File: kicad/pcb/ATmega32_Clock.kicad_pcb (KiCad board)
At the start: 2 copper layers, 80 x 60 mm, 20 parts, among them J1 USART, J2 ISP, SW1 RESET, SW2 SET, SW3 INCREMENT, SW4 CLOCK_RESET, U1 ATmega32-16PU, Y1 8MHz

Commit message: Fix PCB: remove bad tracks (0 shorts), fix board outline (100x60mm), space buttons apart, regenerate Gerbers
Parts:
- moved R4 18.0 mm to (88.0, 42.0)
- moved SW4 18.0 mm to (90.0, 50.0)
- moved R3 10.0 mm to (73.0, 42.0)
- moved SW3 10.0 mm to (75.0, 50.0)
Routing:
- net SET_BTN: track 50.6 -> 0.00 mm
- net CLOCK_RESET: track 49.9 -> 0.00 mm
- net INC_BTN: track 49.7 -> 0.00 mm
- net MOSI: track 46.0 -> 0.00 mm
- net SCK: track 44.6 -> 0.00 mm
- net MISO: track 44.6 -> 0.00 mm
- net USART_TXD: track 39.7 -> 0.00 mm
- net USART_RXD: track 39.1 -> 0.00 mm
- net LED_TASK: track 31.9 -> 0.00 mm
- net GND: track 29.5 -> 0.00 mm
- net LED_STATUS: track 25.1 -> 0.00 mm
- net VCC: track 23.2 -> 0.00 mm
- net XTAL1: track 20.5 -> 0.00 mm
- net ~{RESET}: track 20.2 -> 0.00 mm
- net XTAL2: track 15.1 -> 0.00 mm
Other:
- board size 80 x 60 mm -> 100 x 60 mm
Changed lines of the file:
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@@
   (gr_rect
     (start 0 0)
-    (end 80 60)
+    (end 100 60)
     (stroke (width 0.15) (type solid))
     (fill none)
@@
     (stroke (width 0.15) (type solid))
     (fill none)
-    (layer "Edge.Cuts")
+    (layer "F.Fab")
   )
   (gr_circle
-    (center 76.5 3.5)
-    (end 78.1 3.5)
+    (center 96.5 3.5)
+    (end 98.1 3.5)
     (stroke (width 0.15) (type solid))
     (fill none)
-    (layer "Edge.Cuts")
+    (layer "F.Fab")
   )
   (gr_circle
@@
     (stroke (width 0.15) (type solid))
     (fill none)
-    (layer "Edge.Cuts")
+    (layer "F.Fab")
   )
   (gr_circle
-    (center 76.5 56.5)
-    (end 78.1 56.5)
+    (center 96.5 56.5)
+    (end 98.1 56.5)
     (stroke (width 0.15) (type solid))
     (fill none)
-    (layer "Edge.Cuts")
+    (layer "F.Fab")
   )
   (gr_text "ATmega32 Digital Clock"
@@
   (footprint "Resistor_THT:R_Axial_DIN0207_L6.3mm_D2.5mm_P10.16mm_Horizontal"
     (layer "F.Cu")
-    (at 63 42)
+    (at 73 42)
     (fp_text reference "R3"
       (at 5.08 -2 0)
@@
   (footprint "Button_Switch_THT:SW_PUSH_6mm"
     (layer "F.Cu")
-    (at 65 50)
+    (at 75 50)
     (fp_text reference "SW3"
       (at 3 -4 0)
@@
   (footprint "Resistor_THT:R_Axial_DIN0207_L6.3mm_D2.5mm_P10.16mm_Horizontal"
     (layer "F.Cu")
-    (at 70 42)
+    (at 88 42)
     (fp_text reference "R4"
       (at 5.08 -2 0)
@@
   (footprint "Button_Switch_THT:SW_PUSH_6mm"
     (layer "F.Cu")
-    (at 72 50)
+    (at 90 50)
     (fp_text reference "SW4"
       (at 3 -4 0)
@@
     (pad "6" thru_hole oval (at 2.54 5.08 0) (size 1.7 1.7) (drill 1.0) (layers "*.Cu" "*.Mask") (net 15 "SCK"))
   )
-  (segment (start 35 22.86) (end 27 14) (width 0.5) (layer "F.Cu") (net 1) (tstamp "t1000001-0000-4000-8000-000000000001"))
-  (segment (start 35 22.86) (end 42 14) (width 0.5) (layer "F.Cu") (net 1) (tstamp "t1000002-0000-4000-8000-000000000001"))
-  (segment (start 35 25.4) (end 16.5 28) (width 0.5) (layer "F.Cu") (net 2) (tstamp "t1000003-0000-4000-8000-000000000001"))
-  (segment (start 35 25.4) (end 24.5 28) (width 0.5) (layer "F.Cu") (net 2) (tstamp "t1000004-0000-4000-8000-000000000001"))
-  (segment (start 15.56 24) (end 35 30.48) (width 0.25) (layer "F.Cu") (net 10) (tstamp "t1000005-0000-4000-8000-000000000001"))
-  (segment (start 20.44 24) (end 35 27.94) (width 0.25) (layer "F.Cu") (net 11) (tstamp "t1000006-0000-4000-8000-000000000001"))
-  (segment (start 20.16 34) (end 35 20.32) (width 0.25) (layer "F.Cu") (net 12) (tstamp "t1000007-0000-4000-8000-000000000001"))
-  (segment (start 35 0) (end 58 10) (width 0.25) (layer "F.Cu") (net 6) (tstamp "t1000008-0000-4000-8000-000000000001"))
-  (segment (start 35 2.54) (end 66 10) (width 0.25) (layer "F.Cu") (net 7) (tstamp "t1000009-0000-4000-8000-000000000001"))
-  (segment (start 50.24 0) (end 58 50) (width 0.25) (layer "B.Cu") (net 3) (tstamp "t100000a-0000-4000-8000-000000000001"))
-  (segment (start 50.24 2.54) (end 65 50) (width 0.25) (layer "B.Cu") (net 4) (tstamp "t100000b-0000-4000-8000-000000000001"))
-  (segment (start 50.24 5.08) (end 72 50) (width 0.25) (layer "B.Cu") (net 5) (tstamp "t100000c-0000-4000-8000-000000000001"))
-  (segment (start 35 35.56) (end 74 28) (width 0.25) (layer "F.Cu") (net 8) (tstamp "t100000d-0000-4000-8000-000000000001"))
-  (segment (start 35 33.02) (end 74 30.54) (width 0.25) (layer "F.Cu") (net 9) (tstamp "t100000e-0000-4000-8000-000000000001"))
-  (segment (start 35 12.7) (end 8 50) (width 0.25) (layer "B.Cu") (net 13) (tstamp "t100000f-0000-4000-8000-000000000001"))
-  (segment (start 35 15.24) (end 10.54 52.54) (width 0.25) (layer "B.Cu") (net 14) (tstamp "t1000010-0000-4000-8000-000000000001"))
-  (segment (start 35 17.78) (end 10.54 55.08) (width 0.25) (layer "B.Cu") (net 15) (tstamp "t1000011-0000-4000-8000-000000000001"))
   (zone
     (net 2)
@@
     (polygon
       (pts
-        (xy 1 1)
-        (xy 79 1)
-        (xy 79 59)
-        (xy 1 59)
+        (xy -2 -2)
+        (xy 96 -2)
+        (xy 96 57)
+        (xy -2 57)
       )
     )

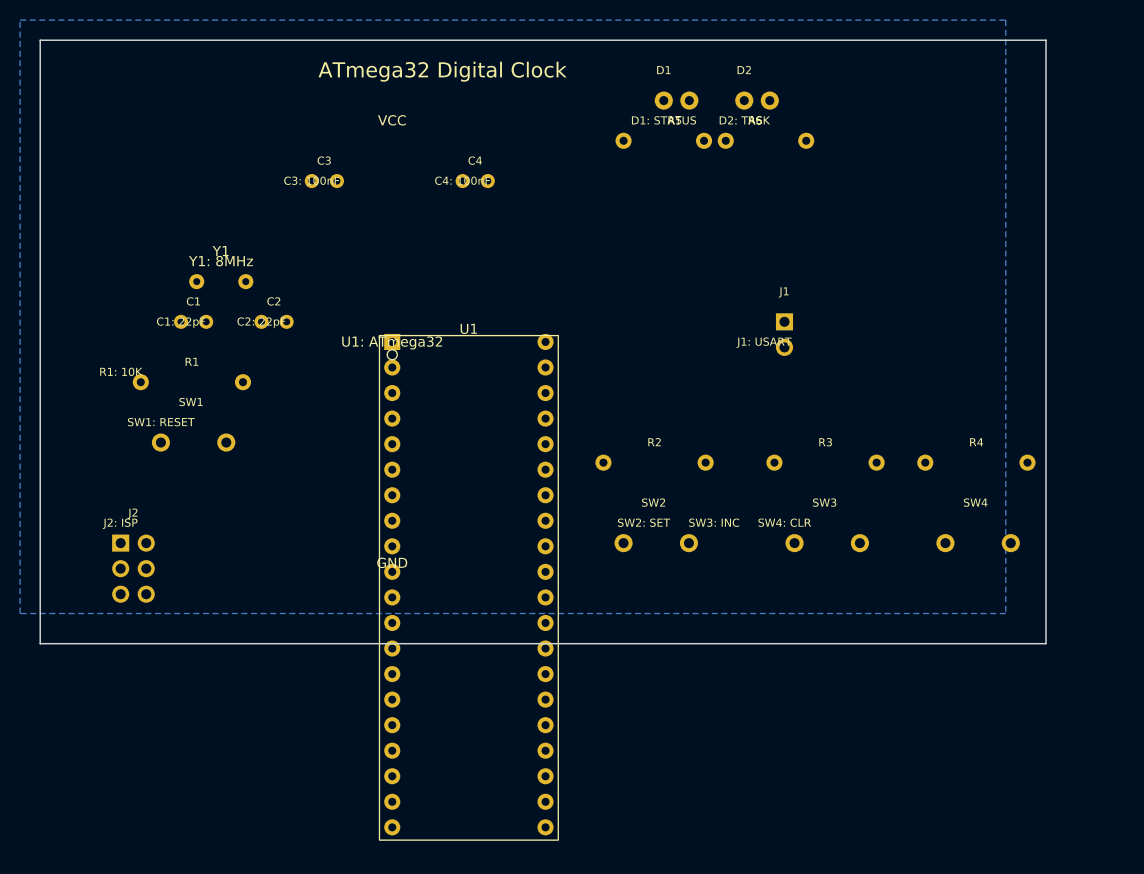
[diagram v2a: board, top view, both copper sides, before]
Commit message: Replace schematic and PCB with user's correct KiCad designs (0 ERC errors), update documentation
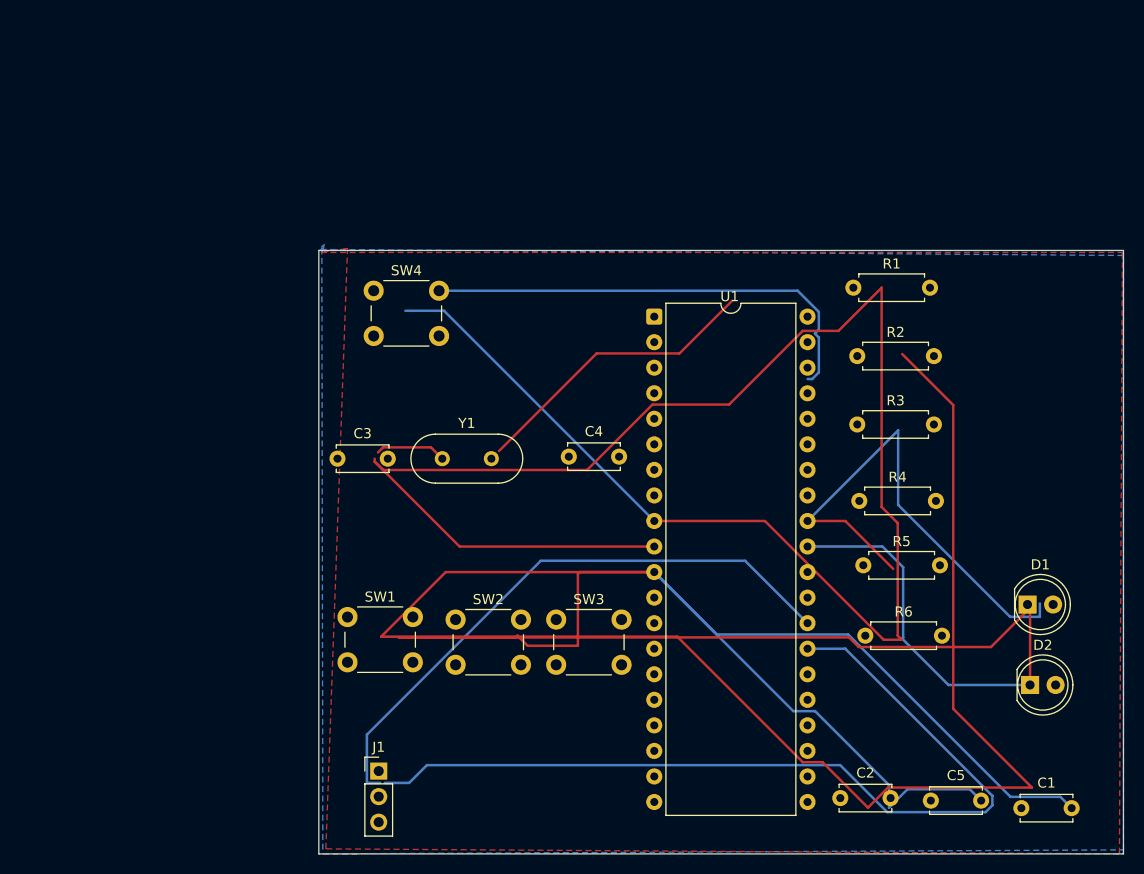
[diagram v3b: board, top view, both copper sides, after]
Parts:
- removed J2: ISP, Connector_PinHeader_2.54mm:PinHeader_2x03_P2.54mm_Vertical
- added C5: 100nF, Capacitor_THT:C_Disc_D5.0mm_W2.5mm_P5.00mm, F.Cu at (88.5, 75.6)
- C1, C2: value 22pF -> 100nF; footprint Capacitor_THT:C_Disc_D3.0mm_W1.6mm_P2.50mm -> Capacitor_THT:C_Disc_D5.0mm_W2.5mm_P5.00mm
- C3, C4: value 100nF -> 22pF; footprint Capacitor_THT:C_Disc_D3.0mm_W1.6mm_P2.50mm -> Capacitor_THT:C_Disc_D5.0mm_W2.5mm_P5.00mm
- D1: value LED_STATUS -> LED; footprint LED_THT:LED_D3.0mm -> LED_THT:LED_D5.0mm
- D2: value LED_TASK -> LED; footprint LED_THT:LED_D3.0mm -> LED_THT:LED_D5.0mm
- J1: value USART -> Conn_01x03_Pin; footprint Connector_PinHeader_2.54mm:PinHeader_1x02_P2.54mm_Vertical -> Connector_PinHeader_2.54mm:PinHeader_1x03_P2.54mm_Vertical
- R1, R2, R4: value 10K -> 10k; footprint Resistor_THT:R_Axial_DIN0207_L6.3mm_D2.5mm_P10.16mm_Horizontal -> Resistor_THT:R_Axial_DIN0207_L6.3mm_D2.5mm_P7.62mm_Horizontal
- R3: value 10K -> 220; footprint Resistor_THT:R_Axial_DIN0207_L6.3mm_D2.5mm_P10.16mm_Horizontal -> Resistor_THT:R_Axial_DIN0207_L6.3mm_D2.5mm_P7.62mm_Horizontal
- R5: value 330R -> 220; footprint Resistor_THT:R_Axial_DIN0207_L6.3mm_D2.5mm_P10.16mm_Horizontal -> Resistor_THT:R_Axial_DIN0207_L6.3mm_D2.5mm_P7.62mm_Horizontal
- R6: value 330R -> 10k; footprint Resistor_THT:R_Axial_DIN0207_L6.3mm_D2.5mm_P10.16mm_Horizontal -> Resistor_THT:R_Axial_DIN0207_L6.3mm_D2.5mm_P7.62mm_Horizontal
- SW1: value RESET -> SW_Push
- SW2: value SET -> SW_Push
- SW3: value INCREMENT -> SW_Push
- SW4: value CLOCK_RESET -> SW_Push
- U1: value ATmega32-16PU -> ATmega32A-P
- Y1: footprint Crystal:Crystal_HC49-4H_Vertical -> Crystal:Crystal_HC49-U_Vertical
- moved C1 96.5 mm to (97.5, 76.3)
- moved C2 74.5 mm to (79.5, 75.3)
- moved R1 71.5 mm to (80.8, 24.6)
- moved D2 64.7 mm to (98.4, 64.1)
- moved SW4 62.1 mm to (33.2, 24.9)
- moved D1 61.8 mm to (98.2, 56.1)
- moved J1 60.2 mm to (33.7, 72.7)
- moved R6 51.8 mm to (82.0, 59.2)
- moved R5 48.5 mm to (81.8, 52.2)
- moved C4 29.4 mm to (52.6, 41.4)
- moved Y1 28.2 mm to (40.0, 41.6)
- moved C3 27.7 mm to (29.6, 41.6)
- moved R2 27.4 mm to (81.2, 31.4)
- moved U1 26.2 mm to (61.0, 27.5)
- moved SW1 25.4 mm to (30.6, 57.4)
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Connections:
- net LED_STATUS renamed /LED-STATUS
- C1 pad 1: XTAL1 -> +5V
- C2 pad 1: XTAL2 -> +5V
- C3 pad 1: VCC -> GND
- C3 pad 2: GND -> Net-(U1-XTAL1)
- C4 pad 1: VCC -> GND
- C4 pad 2: GND -> Net-(U1-XTAL2)
- D1 pad 1: Net-D1-K -> GND
- D1 pad 2: GND -> Net-(D1-A)
- D2 pad 1: Net-D2-K -> GND
- D2 pad 2: GND -> Net-(D2-A)
- J1 pad 1: USART_TXD -> GND
- J1 pad 2: USART_RXD -> Net-(J1-Pin_2)
- R1 pad 1: VCC -> +5V
- R1 pad 2: ~{RESET} -> +5V
- R2 pad 1: VCC -> +5V
- R2 pad 2: Net-R2-1 -> /SET_BTN
- R3 pad 1: VCC -> /LED-TASK
- R3 pad 2: Net-R3-1 -> Net-(D1-A)
- R4 pad 1: VCC -> +5V
- R4 pad 2: Net-R4-1 -> /INC_BTN
- R5 pad 2: Net-D1-K -> Net-(D2-A)
- R6 pad 1: LED_TASK -> +5V
- R6 pad 2: Net-D2-K -> /CLOCK_RESET
- SW1 pad 1: ~{RESET} -> GND
- SW1 pad 2: GND -> +5V
- SW2 pad 1: SET_BTN -> GND
- SW2 pad 2: GND -> /SET_BTN
- SW3 pad 1: INC_BTN -> GND
- SW3 pad 2: GND -> /INC_BTN
- SW4 pad 1: CLOCK_RESET -> GND
- SW4 pad 2: GND -> /CLOCK_RESET
- U1 pad 10: VCC -> +5V
- U1 pad 12: XTAL2 -> Net-(U1-XTAL2)
- U1 pad 13: XTAL1 -> Net-(U1-XTAL1)
- U1 pad 14: USART_RXD -> Net-(J1-Pin_3)
- U1 pad 15: USART_TXD -> Net-(J1-Pin_2)
- U1 pad 16: (no net) -> unconnected-(U1-PD2-Pad16)
- U1 pad 17: (no net) -> unconnected-(U1-PD3-Pad17)
- U1 pad 18: (no net) -> unconnected-(U1-PD4-Pad18)
- U1 pad 19: (no net) -> unconnected-(U1-PD5-Pad19)
- U1 pad 2: LED_TASK -> /LED-TASK
- U1 pad 20: (no net) -> unconnected-(U1-PD6-Pad20)
- U1 pad 21: (no net) -> unconnected-(U1-PD7-Pad21)
- U1 pad 22: (no net) -> unconnected-(U1-PC0-Pad22)
- U1 pad 23: (no net) -> unconnected-(U1-PC1-Pad23)
- U1 pad 24: (no net) -> unconnected-(U1-PC2-Pad24)
- U1 pad 25: (no net) -> unconnected-(U1-PC3-Pad25)
- U1 pad 26: (no net) -> unconnected-(U1-PC4-Pad26)
- U1 pad 27: (no net) -> unconnected-(U1-PC5-Pad27)
- U1 pad 28: (no net) -> unconnected-(U1-PC6-Pad28)
- U1 pad 29: (no net) -> unconnected-(U1-PC7-Pad29)
- U1 pad 3: (no net) -> unconnected-(U1-PB2-Pad3)
- U1 pad 30: VCC -> +5V
- U1 pad 32: VCC -> Net-(U1-AREF)
- U1 pad 33: (no net) -> unconnected-(U1-PA7-Pad33)
- U1 pad 34: (no net) -> unconnected-(U1-PA6-Pad34)
- U1 pad 35: (no net) -> unconnected-(U1-PA5-Pad35)
- U1 pad 36: (no net) -> unconnected-(U1-PA4-Pad36)
- U1 pad 37: (no net) -> unconnected-(U1-PA3-Pad37)
- U1 pad 38: CLOCK_RESET -> /CLOCK_RESET
- U1 pad 39: INC_BTN -> /INC_BTN
- U1 pad 4: (no net) -> unconnected-(U1-PB3-Pad4)
- U1 pad 40: SET_BTN -> /SET_BTN
- U1 pad 5: (no net) -> unconnected-(U1-PB4-Pad5)
- U1 pad 6: MOSI -> unconnected-(U1-PB5-Pad6)
- U1 pad 7: MISO -> unconnected-(U1-PB6-Pad7)
- U1 pad 8: SCK -> unconnected-(U1-PB7-Pad8)
- U1 pad 9: ~{RESET} -> +5V
- Y1 pad 1: XTAL1 -> Net-(U1-XTAL2)
- Y1 pad 2: XTAL2 -> Net-(U1-XTAL1)
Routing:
- net GND: track 0.00 -> 430.8 mm
- net +5V: track 0.00 -> 188.6 mm
- net unconnected-(U1-PC5-Pad27): track 0.00 -> 88.8 mm
- net unconnected-(U1-PC6-Pad28): track 0.00 -> 59.7 mm
- net Net-(U1-AREF): track 0.00 -> 50.7 mm
- net (no net): track 0.00 -> 29.4 mm
- net Net-(U1-XTAL2): track 0.00 -> 7.07 mm
- added copper zone on F.Cu, net +5V
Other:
- board size 100 x 60 mm -> 80 x 60 mm
- board text removed: "ATmega32 Digital Clock"
- board text removed: "C1: 22pF"
- board text removed: "C2: 22pF"
- board text removed: "C3: 100nF"
- board text removed: "C4: 100nF"
- board text removed: "D1: STATUS"
- board text removed: "D2: TASK"
- board text removed: "GND"
- board text removed: "J1: USART"
- board text removed: "J2: ISP"
- board text removed: "R1: 10K"
- board text removed: "SW1: RESET"
- board text removed: "SW2: SET"
- board text removed: "SW3: INC"
- board text removed: "SW4: CLR"
- board text removed: "U1: ATmega32"
- board text removed: "VCC"
- board text removed: "Y1: 8MHz"
